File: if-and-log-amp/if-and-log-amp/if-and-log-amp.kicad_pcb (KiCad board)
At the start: 2 copper layers, 91.7 x 48.8 mm, 59 parts, among them J301 Conn_Coaxial, J306 Conn_Coaxial, U301 AD603AQ, U302 L78L05_TO92, U303 LM317L_TO92, U304 AD8307AN, U305 CA3140

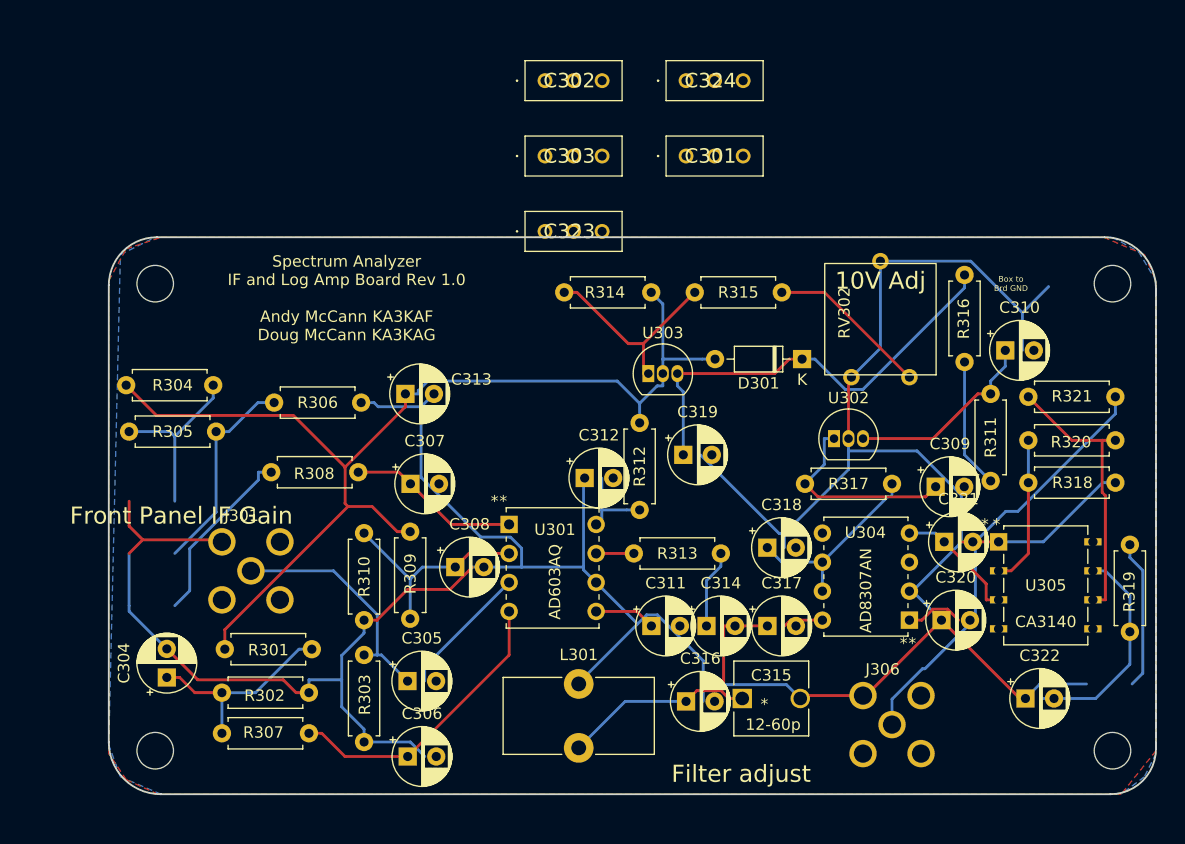
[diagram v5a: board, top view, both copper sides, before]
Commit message: revised if and log amp schematic and board
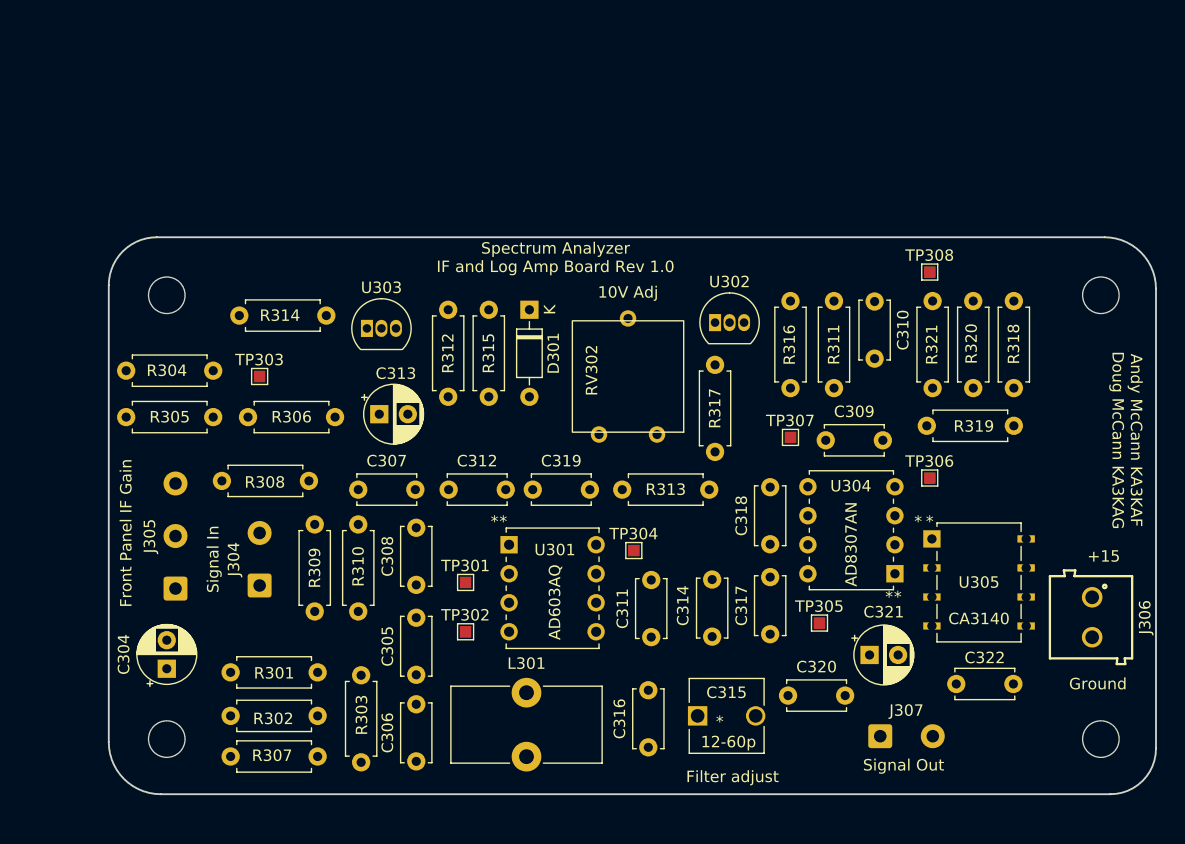
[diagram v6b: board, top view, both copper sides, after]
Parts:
- removed C301, C302, C303: 5n, if-log-amp:DSS1NB32A102Q91A
- removed C323, C324: 1n, if-log-amp:DSS1NB32A102Q91A
- added J305: Conn_01x03, Connector_Wire:SolderWire-0.5sqmm_1x03_P4.6mm_D0.9mm_OD2.1mm, F.Cu at (101.2, 111.2)
- added J306: Conn_01x02, if-log-amp:691103110002, F.Cu at (181.5, 113.7)
- added TP301: TestPoint, TestPoint:TestPoint_Pad_1.0x1.0mm, F.Cu at (126.6, 110.6)
- added TP302: TestPoint, TestPoint:TestPoint_Pad_1.0x1.0mm, F.Cu at (126.6, 115.0)
- added TP303: TestPoint, TestPoint:TestPoint_Pad_1.0x1.0mm, F.Cu at (108.6, 92.6)
- added TP304: TestPoint, TestPoint:TestPoint_Pad_1.0x1.0mm, F.Cu at (141.3, 107.8)
- added TP305: TestPoint, TestPoint:TestPoint_Pad_1.0x1.0mm, F.Cu at (157.6, 114.2)
- added TP306: TestPoint, TestPoint:TestPoint_Pad_1.0x1.0mm, F.Cu at (167.2, 101.5)
- added TP307: TestPoint, TestPoint:TestPoint_Pad_1.0x1.0mm, F.Cu at (155.0, 97.9)
- added TP308: TestPoint, TestPoint:TestPoint_Pad_1.0x1.0mm, F.Cu at (167.2, 83.5)
- C305, C306, C307, C308, C309, C310, C311, C312, C314, C316, C317, C318, C319, C320, C322: footprint Capacitor_THT:CP_Radial_D5.0mm_P2.50mm -> Capacitor_THT:C_Disc_D5.0mm_W2.5mm_P5.00mm
- J304: renamed from J301; value Conn_Coaxial -> Coax Solder Point; footprint if-log-amp:MOLEX_73391-0060 -> Connector_Wire:SolderWire-0.5sqmm_1x02_P4.6mm_D0.9mm_OD2.1mm
- J307: renamed from J306; footprint if-log-amp:MOLEX_73391-0060 -> Connector_Wire:SolderWire-0.5sqmm_1x02_P4.6mm_D0.9mm_OD2.1mm
- moved R314 28.5 mm to (114.4, 87.3)
- moved U303 25.0 mm to (118.0, 88.4)
- moved D301 24.3 mm to (132.2, 86.8), turned to -90 degrees
- moved RV302 22.7 mm to (143.4, 97.4)
- moved R319 20.7 mm to (174.6, 96.9), turned to 180 degrees
- moved R315 20.2 mm to (128.6, 94.4), turned to 90 degrees
- moved R312 19.5 mm to (125.1, 86.8)
- moved R311 15.9 mm to (158.9, 93.6)
- moved R316 15.4 mm to (155.0, 93.6)
- moved C320 15.0 mm to (154.8, 120.5)
- moved U302 14.5 mm to (148.4, 87.9)
- moved C319 13.5 mm to (132.5, 102.5)
- moved R320 13.3 mm to (171.0, 93.6), turned to 90 degrees
- moved R317 13.1 mm to (148.4, 91.6), turned to -90 degrees
- moved C310 12.2 mm to (162.4, 86.0), turned to -90 degrees
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- renumbered R310 to R309, R309 to R310
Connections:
- C305 pad 1: Net-(C305-Pad1) -> /In
- J304 pad 1: Net-(C305-Pad1) -> /In
- J307 pad 1: /Out -> Net-(C323-Pad1)
- R303 pad 1: Net-(C305-Pad1) -> /In
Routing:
- net GND: track 401.8 -> 0.00 mm
- net +10: track 97.1 -> 0.00 mm
- net Net-(C319-Pad1): track 38.9 -> 0.00 mm
- net Net-(C314-Pad2): track 26.3 -> 0.00 mm
- net +15: track 24.4 -> 0.00 mm
- net Net-(R320-Pad1): track 24.4 -> 0.00 mm
- net Net-(C305-Pad1): track 20.9 -> 0.00 mm
- net Net-(C322-Pad2): track 19.0 -> 0.00 mm
- net Net-(C304-Pad1): track 18.4 -> 0.00 mm
- net Net-(C303-Pad3): track 18.3 -> 0.00 mm
- net Net-(R314-Pad2): track 18.2 -> 0.00 mm
- net Net-(C318-Pad1): track 17.5 -> 0.00 mm
- net Net-(C310-Pad1): track 17.1 -> 0.00 mm
- net Net-(C302-Pad3): track 15.8 -> 0.00 mm
- net Net-(C301-Pad3): track 15.7 -> 0.00 mm
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- removed copper zone on B.Cu, net GND
- removed copper zone on F.Cu, net GND
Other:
- board text added: "+15"
- board text added: "Andy McCann KA3KAF Doug McCann KA3KAG"
- board text added: "Ground"
- board text added: "Signal In"
- board text added: "Signal Out"
- board text added: "Spectrum Analyzer IF and Log Amp Board Rev 1.0"
- board text removed: "Box to Brd GND"
- board text removed: "Spectrum Analyzer IF and Log Amp Board Rev 1.0 Andy McCann KA3KAF Doug McCann KA3KAG"

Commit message: updates to if log amp and resolution filter boards
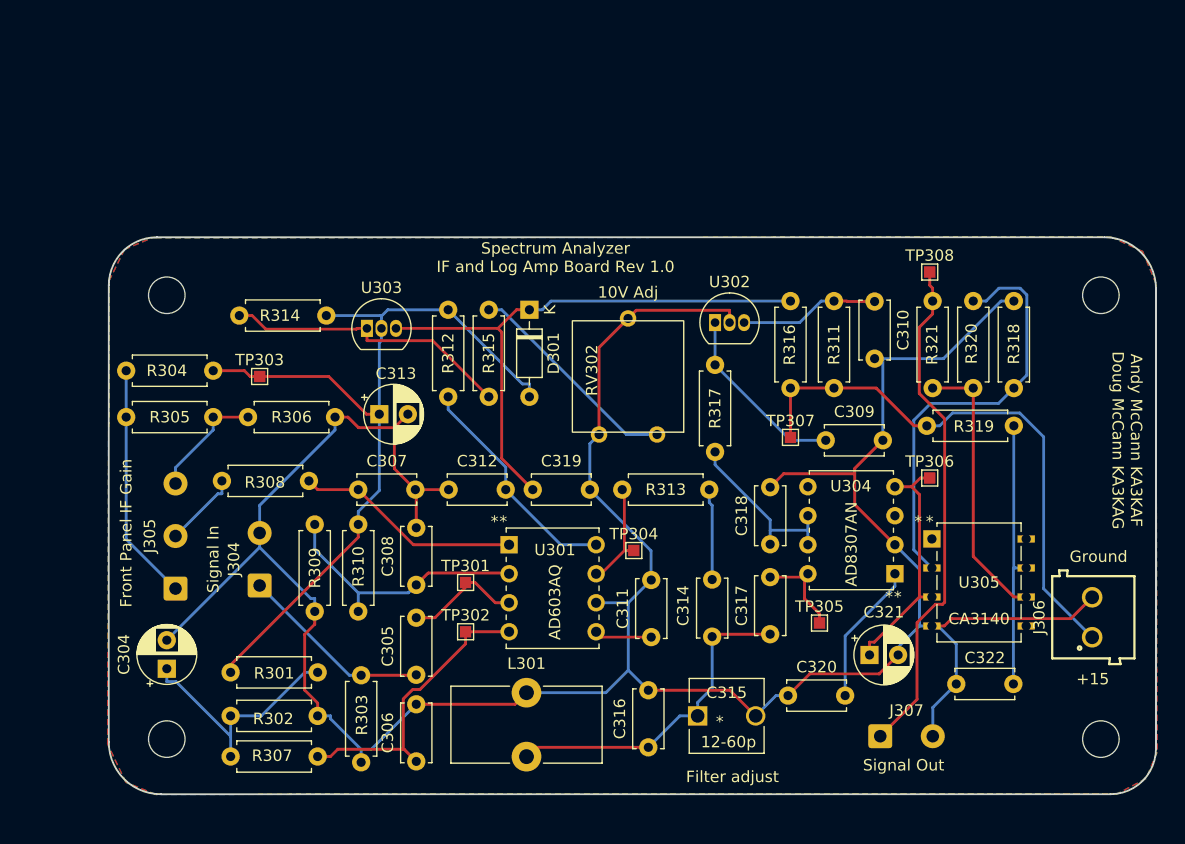
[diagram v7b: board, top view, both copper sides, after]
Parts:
- turned J306 to 90 degrees
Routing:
- net GND: track 0.00 -> 251.6 mm
- net +10: track 0.00 -> 74.6 mm
- net Net-(C319-Pad1): track 0.00 -> 50.9 mm
- net +15: track 0.00 -> 48.5 mm
- net Net-(C323-Pad1): track 0.00 -> 44.9 mm
- net Net-(R318-Pad1): track 0.00 -> 37.6 mm
- net Net-(C314-Pad2): track 0.00 -> 29.1 mm
- net Net-(C306-Pad1): track 0.00 -> 26.1 mm
- net Net-(R314-Pad2): track 0.00 -> 25.5 mm
- net Net-(R320-Pad1): track 0.00 -> 24.4 mm
- net Net-(C322-Pad2): track 0.00 -> 23.7 mm
- net Net-(C308-Pad1): track 0.00 -> 23.2 mm
- net Net-(C321-Pad1): track 0.00 -> 21.5 mm
- net Net-(C304-Pad1): track 0.00 -> 21.4 mm
- net Net-(C301-Pad3): track 0.00 -> 20.9 mm
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- added copper zone on B.Cu, net GND
- added copper zone on F.Cu, net GND

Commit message: Add amp to if-and-log-amp
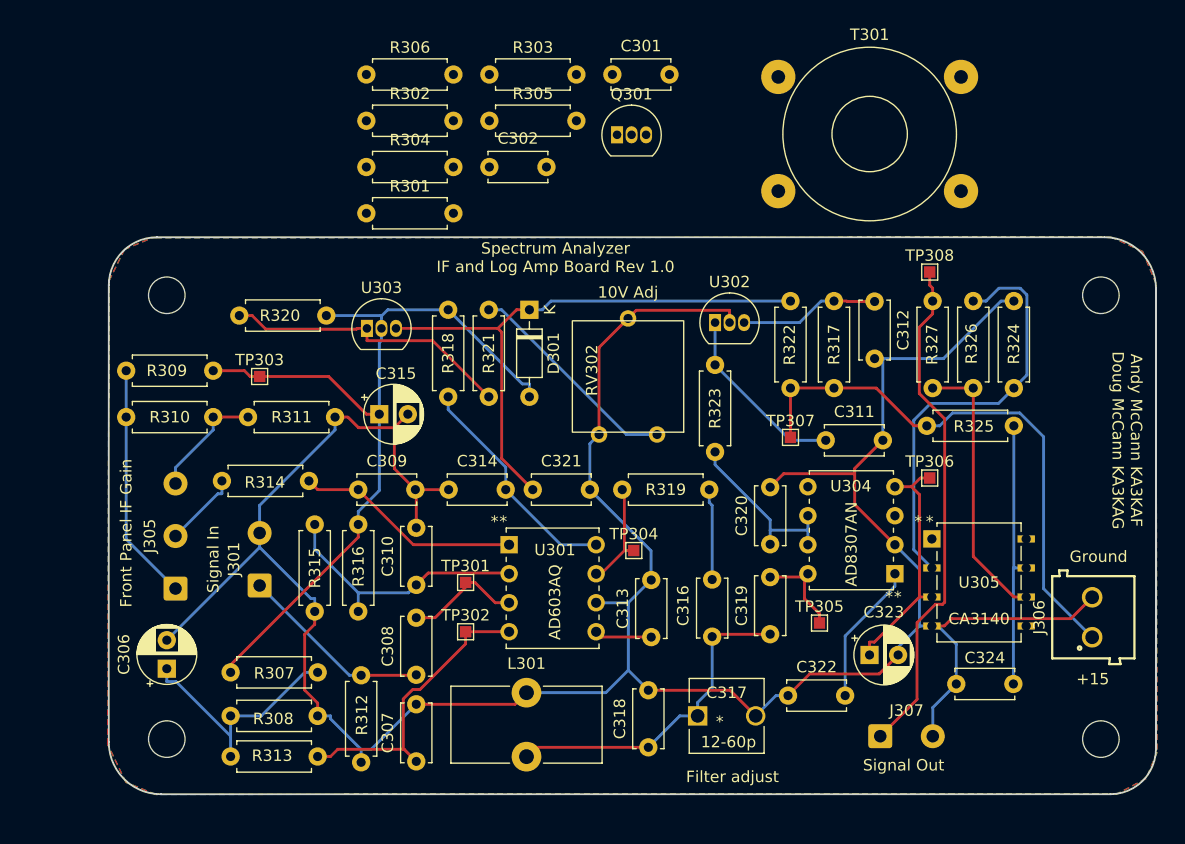
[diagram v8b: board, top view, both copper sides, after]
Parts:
- added C301: .1u, Capacitor_THT:C_Disc_D5.0mm_W2.5mm_P5.00mm, F.Cu at (139.4, 66.2)
- added C302: .1u, Capacitor_THT:C_Disc_D5.0mm_W2.5mm_P5.00mm, F.Cu at (128.7, 74.3)
- added Q301: 2N3904, Package_TO_SOT_THT:TO-92_Inline, F.Cu at (139.9, 71.4)
- added R301: 10k, Resistor_THT:R_Axial_DIN0207_L6.3mm_D2.5mm_P7.62mm_Horizontal, F.Cu at (117.9, 78.3)
- added R302: 2k, Resistor_THT:R_Axial_DIN0207_L6.3mm_D2.5mm_P7.62mm_Horizontal, F.Cu at (117.9, 70.2)
- added R303: 47, Resistor_THT:R_Axial_DIN0207_L6.3mm_D2.5mm_P7.62mm_Horizontal, F.Cu at (128.7, 66.2)
- added R304: 100, Resistor_THT:R_Axial_DIN0207_L6.3mm_D2.5mm_P7.62mm_Horizontal, F.Cu at (117.9, 74.3)
- added R305: 100, Resistor_THT:R_Axial_DIN0207_L6.3mm_D2.5mm_P7.62mm_Horizontal, F.Cu at (128.7, 70.2)
- added R306: 470, Resistor_THT:R_Axial_DIN0207_L6.3mm_D2.5mm_P7.62mm_Horizontal, F.Cu at (117.9, 66.2)
- added T301: FT37-43 8:2 t, Transformer_THT:Transformer_Toroid_Horizontal_D14.0mm_Amidon-T50, F.Cu at (154.0, 76.4)
- J301: renamed from J304; value Coax Solder Point -> Coax
- renumbered C304 to C306, C306 to C307, C305 to C308, C307 to C309, C308 to C310, C309 to C311, C310 to C312, C311 to C313, C312 to C314, C313 to C315, C314 to C316, C315 to C317, C316 to C318, C317 to C319, C318 to C320, C319 to C321, C320 to C322, C321 to C323, C322 to C324, R301 to R307, R302 to R308, R304 to R309, R305 to R310, R306 to R311, R303 to R312, R307 to R313, R308 to R314, R309 to R315, R310 to R316, R311 to R317, R312 to R318, R313 to R319, R314 to R320, R315 to R321, R316 to R322, R317 to R323, R318 to R324, R319 to R325, R320 to R326, R321 to R327
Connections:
- net +10 renamed /+10
- net +15 renamed /+15
- net +5 renamed /+5
- C308 pad 1: /In -> Net-(C308-Pad1)
- R312 pad 1: /In -> Net-(C308-Pad1)
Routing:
- net Net-(C308-Pad1): track 0.00 -> 17.0 mm
- net /In: track 17.0 -> 0.00 mm
